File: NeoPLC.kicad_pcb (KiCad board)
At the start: 2 copper layers, 75 x 110 mm, 39 parts, among them J1 Backplane 2x6, J2 DI1-4+COM 3.5mm, J3 DI5-8+COM 3.5mm, J4 SWD, U1 STM32G071CBT6, U2 AP2112K-3.3, U3 ISL3178EIBZ, U4 TLP291-4, U5 TLP291-4, Y1 8MHz

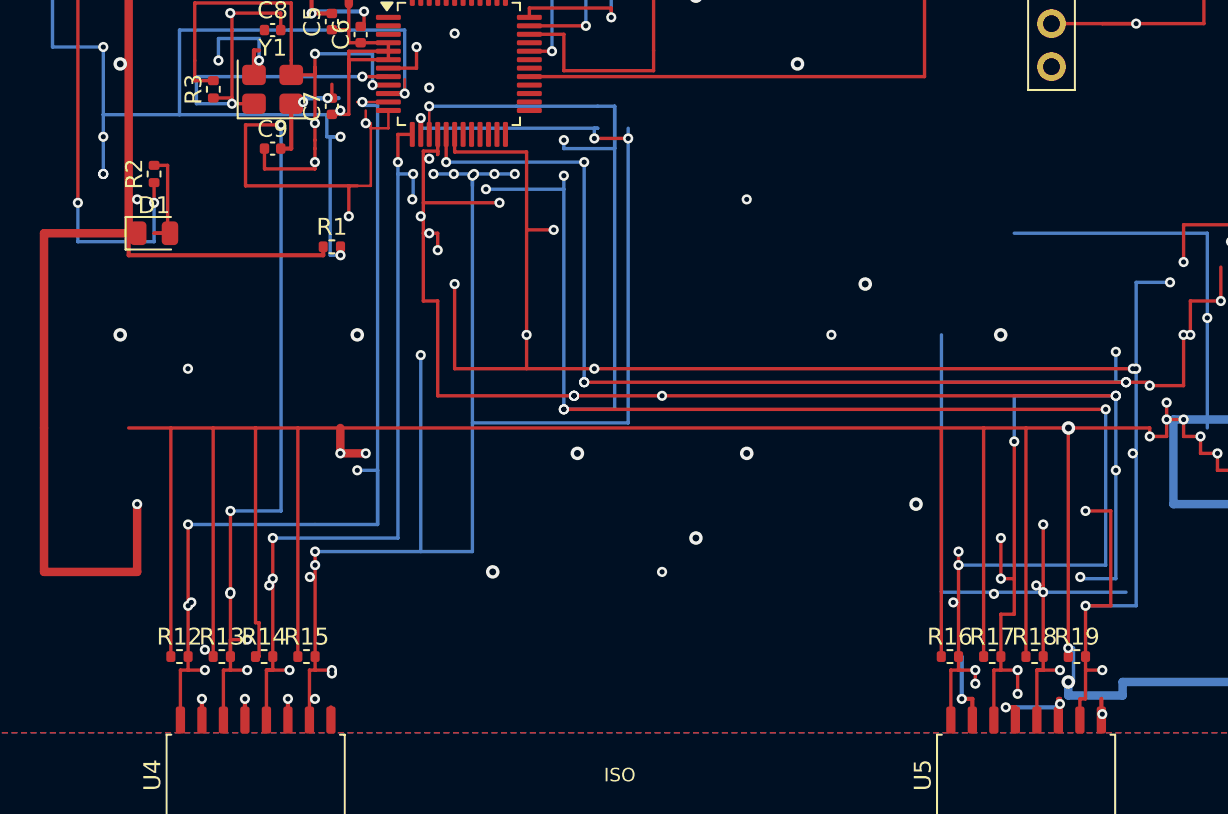
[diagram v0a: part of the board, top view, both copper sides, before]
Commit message: GND adaları kapandı; DI7/+3V3 ve RST kaçışı: DRC 16, kısa yok.
Co-authored-by: Cursor <cursoragent@cursor.com>
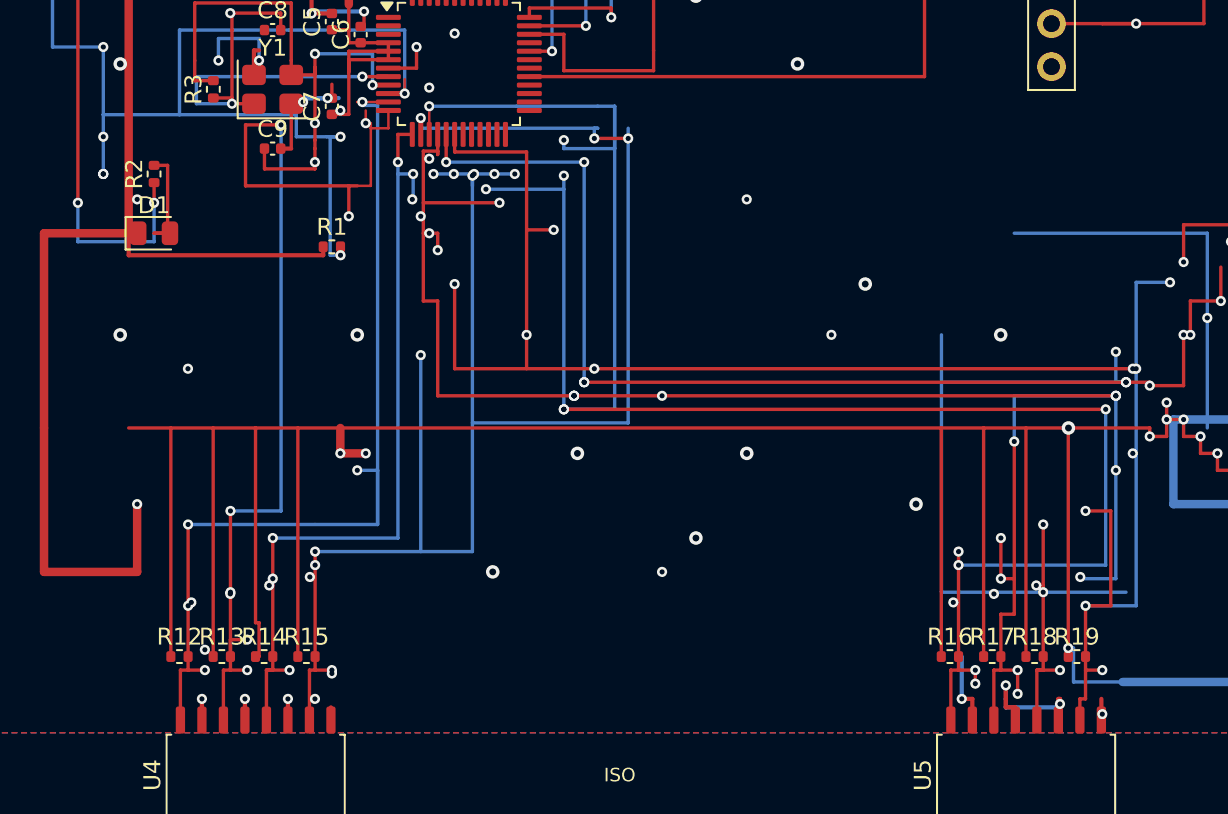
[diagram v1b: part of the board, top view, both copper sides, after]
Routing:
- net GND: track 135.3 -> 137.9 mm
- net +3V3: track 427.0 -> 424.8 mm, vias 24 -> 23
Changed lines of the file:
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@@
 		(net "+3V3")
 	)
-	(via
-		(at 63.99 68.5)
-		(size 0.8)
-		(drill 0.4)
-		(layers "F.Cu" "B.Cu")
-		(net "+3V3")
-	)
 	(segment
 		(start 64.5 22)
@@
 	)
 	(segment
-		(start 63.99 68.5)
-		(end 64.3 68.5)
-		(width 0.2)
-		(layer "B.Cu")
-		(net "+3V3")
-	)
-	(segment
 		(start 70.2 53)
 		(end 70.2 58)
@@
 	(segment
 		(start 67.2 68.5)
-		(end 67.2 69.3)
-		(width 0.5)
-		(layer "B.Cu")
-		(net "+3V3")
-	)
-	(segment
-		(start 63.99 69.3)
-		(end 63.99 68.5)
-		(width 0.5)
+		(end 64.3 68.5)
+		(width 0.2)
 		(layer "B.Cu")
 		(net "+3V3")
@@
 	)
 	(segment
-		(start 67.2 69.3)
-		(end 63.99 69.3)
-		(width 0.5)
-		(layer "B.Cu")
-		(net "+3V3")
-	)
-	(segment
 		(start 64.3 66.5)
 		(end 63.99 66.5)
@@
 	)
 	(segment
+		(start 18.1 37)
+		(end 18.1 34.35)
+		(width 0.2)
+		(layer "F.Cu")
+		(net "GND")
+	)
+	(segment
 		(start 3.5 62)
 		(end 9 62)
@@
 	)
 	(segment
+		(start 60.3 70)
+		(end 60.3 69.5)
+		(width 0.25)
+		(layer "F.Cu")
+		(net "GND")
+	)
+	(segment
 		(start 60.865 70)
 		(end 60.3 70)
@@
 	)
 	(segment
-		(start 18.1 37)
-		(end 18.1 34.35)
-		(width 0.25)
-		(layer "F.Cu")
-		(net "GND")
-	)
-	(segment
 		(start 12.825 70.75)
 		(end 12.825 69.5)
@@
 	)
 	(segment
+		(start 60.3 69.5)
+		(end 60.3 68.7)
+		(width 0.25)
+		(layer "F.Cu")
+		(net "GND")
+	)
+	(segment
 		(start 15.48 14)
 		(end 16.8625 14)
@@
 	)
 	(via
-		(at 60.3 70)
-		(size 0.6)
-		(drill 0.3)
-		(layers "F.Cu" "B.Cu")
-		(net "GND")
-	)
-	(via
 		(at 57.7 69.5)
 		(size 0.6)
@@
 		(net "GND")
 	)
+	(via
+		(at 60.3 68.7)
+		(size 0.6)
+		(drill 0.3)
+		(layers "F.Cu" "B.Cu")
+		(net "GND")
+	)
 	(segment
 		(start 22.4 28.9)
@@
 	)
 	(segment
+		(start 60.3 69.5)
+		(end 60.3 68.7)
+		(width 0.25)
+		(layer "B.Cu")
+		(net "GND")
+	)
+	(segment
+		(start 60.3 69.5)
+		(end 60.3 70)
+		(width 0.25)
+		(layer "B.Cu")
+		(net "GND")
+	)
+	(segment
 		(start 60.3 70)
 		(end 63.5 70)
@@
 	)
 	(segment
-		(start 20.2 35)
-		(end 20.2 36.3)
-		(width 0.2)
-		(layer "B.Cu")
-		(net "/Node Core/MOD_RST#")
-	)
-	(segment
 		(start 11.5 30)
 		(end 11.5 35)
@@
 	)
 	(segment
+		(start 7 35)
+		(end 18.4 35)
+		(width 0.2)
+		(layer "B.Cu")
+		(net "/Node Core/MOD_RST#")
+	)
+	(segment
 		(start 4 31)
 		(end 7 31)
@@
 	)
 	(segment
-		(start 7 35)
-		(end 20.2 35)
-		(width 0.2)
-		(layer "B.Cu")
-		(net "/Node Core/MOD_RST#")
-	)
-	(segment
 		(start 4 23)
 		(end 4 31)
@@
 	)
 	(segment
+		(start 18.4 36.3)
+		(end 20.2 36.3)
+		(width 0.2)
+		(layer "B.Cu")
+		(net "/Node Core/MOD_RST#")
+	)
+	(segment
 		(start 7 6)
 		(end 7 14.5)
@@
 	)
 	(segment
+		(start 18.4 35)
+		(end 18.4 36.3)
+		(width 0.2)
+		(layer "B.Cu")
+		(net "/Node Core/MOD_RST#")
+	)
+	(segment
 		(start 38.77 6)
 		(end 56 6)
@@
 	)
 	(via
-		(at 19.2 62.3)
+		(at 25.75 35.2)
 		(size 0.6)
 		(drill 0.3)
@@
 	)
 	(via
-		(at 25.75 35.2)
+		(at 19.2 62.3)
 		(size 0.6)
 		(drill 0.3)

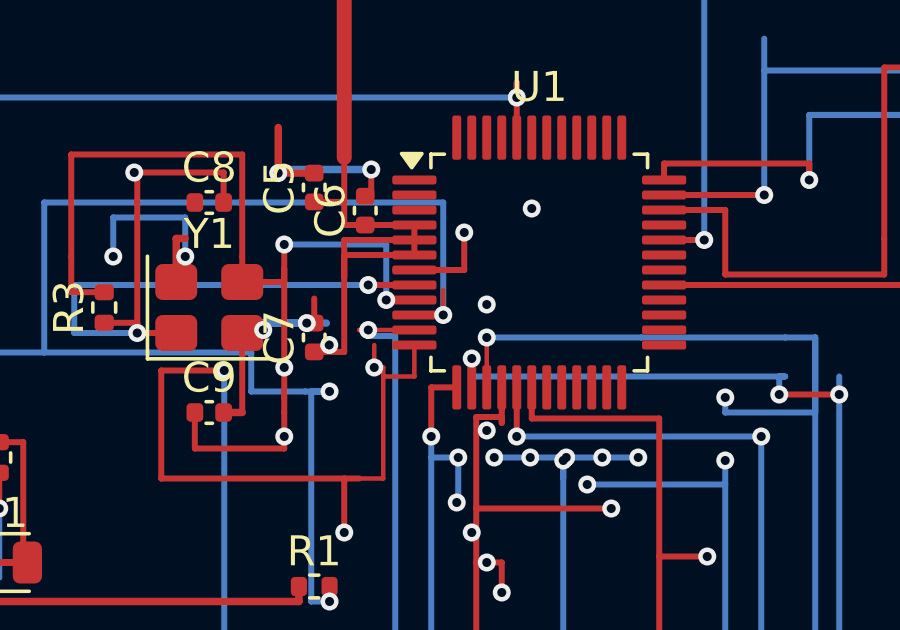
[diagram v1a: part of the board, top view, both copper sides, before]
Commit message: RST via doğuya alındı; pad9 kaçışı kapandı, kısa yok.
Co-authored-by: Cursor <cursoragent@cursor.com>
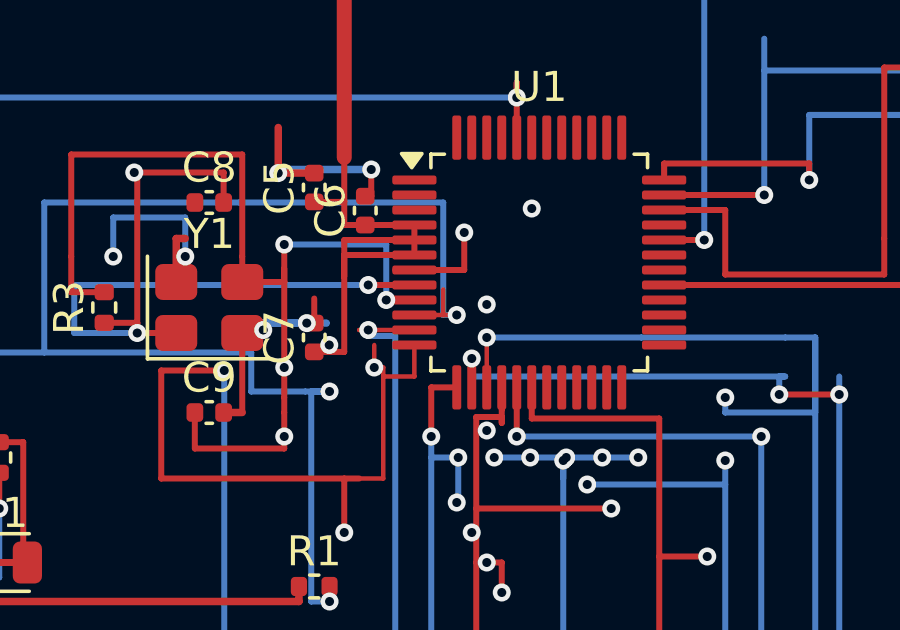
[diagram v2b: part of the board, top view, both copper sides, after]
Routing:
- net /Node Core/MOD_RST#: track 255.2 -> 256.1 mm
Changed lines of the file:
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@@
+	)
+	(segment
+		(start 22.3 32.75)
+		(end 23.8375 32.75)
+		(width 0.2)
+		(layer "F.Cu")
+		(net "/Node Core/HSE_IN")
 	)
 	(segment
@@
 		(start 17.48 29)
 		(end 17.48 30)
-		(width 0.2)
-		(layer "F.Cu")
-		(net "/Node Core/HSE_IN")
-	)
-	(segment
-		(start 22.3 32.75)
-		(end 23.8375 32.75)
 		(width 0.2)
 		(layer "F.Cu")
@@
 		(net "/Node Core/MOD_RST#")
 	)
+	(segment
+		(start 24.8 33.75)
+		(end 25.25 33.75)
+		(width 0.15)
+		(layer "F.Cu")
+		(net "/Node Core/MOD_RST#")
+	)
+	(via
+		(at 25.25 33.75)
+		(size 0.6)
+		(drill 0.3)
+		(layers "F.Cu" "B.Cu")
+		(net "/Node Core/MOD_RST#")
+	)
 	(via
 		(at 66 23)
@@
 	(via
 		(at 21.01 36.3)
-		(size 0.6)
-		(drill 0.3)
-		(layers "F.Cu" "B.Cu")
-		(net "/Node Core/MOD_RST#")
-	)
-	(via
-		(at 24.8 33.75)
 		(size 0.6)
 		(drill 0.3)
@@
 		(width 0.2)
 		(layer "B.Cu")
+		(net "/Node Core/MOD_RST#")
+	)
+	(segment
+		(start 24.8 33.75)
+		(end 25.25 33.75)
+		(width 0.2)
+		(layer "B.Cu")

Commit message: Y1 pad4 C8 GND’ye bağlandı; kristal pad2 adası duruyor.
Co-authored-by: Cursor <cursoragent@cursor.com>
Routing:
- net GND: track 137.9 -> 139.5 mm, vias 38 -> 39
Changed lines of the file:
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@@
+	)
+	(segment
+		(start 16.52 31.2)
+		(end 16.52 30)
+		(width 0.2)
+		(layer "F.Cu")
+		(net "GND")
 	)
 	(segment
@@
 		(end 57.7 69.5)
 		(width 0.25)
+		(layer "F.Cu")
+		(net "GND")
+	)
+	(segment
+		(start 16.2 31.2)
+		(end 16.52 31.2)
+		(width 0.2)
 		(layer "F.Cu")
 		(net "GND")
@@
 	)
 	(via
+		(at 18.1 37)
+		(size 0.6)
+		(drill 0.3)
+		(layers "F.Cu" "B.Cu")
+		(net "GND")
+	)
+	(via
 		(at 35 55)
 		(size 0.8)
@@
 	)
 	(via
+		(at 19.5 31.4)
+		(size 0.6)
+		(drill 0.3)
+		(layers "F.Cu" "B.Cu")
+		(net "/Node Core/HSE_OUT")
+	)
+	(via
+		(at 19.5 35.5)
+		(size 0.6)
+		(drill 0.3)
+		(layers "F.Cu" "B.Cu")
+		(net "/Node Core/HSE_OUT")
+	)
+	(via
+		(at 19.5 37.8)
+		(size 0.6)
+		(drill 0.3)
+		(layers "F.Cu" "B.Cu")
+		(net "/Node Core/HSE_OUT")
+	)
+	(via
 		(at 22.9 33.25)
 		(size 0.6)
 		(drill 0.3)
-		(layers "F.Cu" "B.Cu")
-		(net "/Node Core/HSE_OUT")
-	)
-	(via
-		(at 19.5 31.4)
-		(size 0.6)
-		(drill 0.3)
-		(layers "F.Cu" "B.Cu")
-		(net "/Node Core/HSE_OUT")
-	)
-	(via
-		(at 19.5 35.5)
-		(size 0.6)
-		(drill 0.3)
-		(layers "F.Cu" "B.Cu")
-		(net "/Node Core/HSE_OUT")
-	)
-	(via
-		(at 19.5 37.8)
-		(size 0.6)
-		(drill 0.3)
